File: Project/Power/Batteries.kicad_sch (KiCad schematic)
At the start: 52 parts, among them J10 Battery, J11 Battery, J12 Battery, J9 Battery, Q3 SQJ138ELP, Q4 SQJ138ELP, Q5 SQJ138ELP, Q6 SQJ138ELP, U10 INA199B3DCKR, U11 TL331, U12 INA199B3DCKR, U13 TL331, U2 NCV68061, U3 NCV68061, U4 INA199B3DCKR, U5 TL331, U6 INA199B3DCKR, U7 TL331, U8 NCV68061, U9 NCV68061

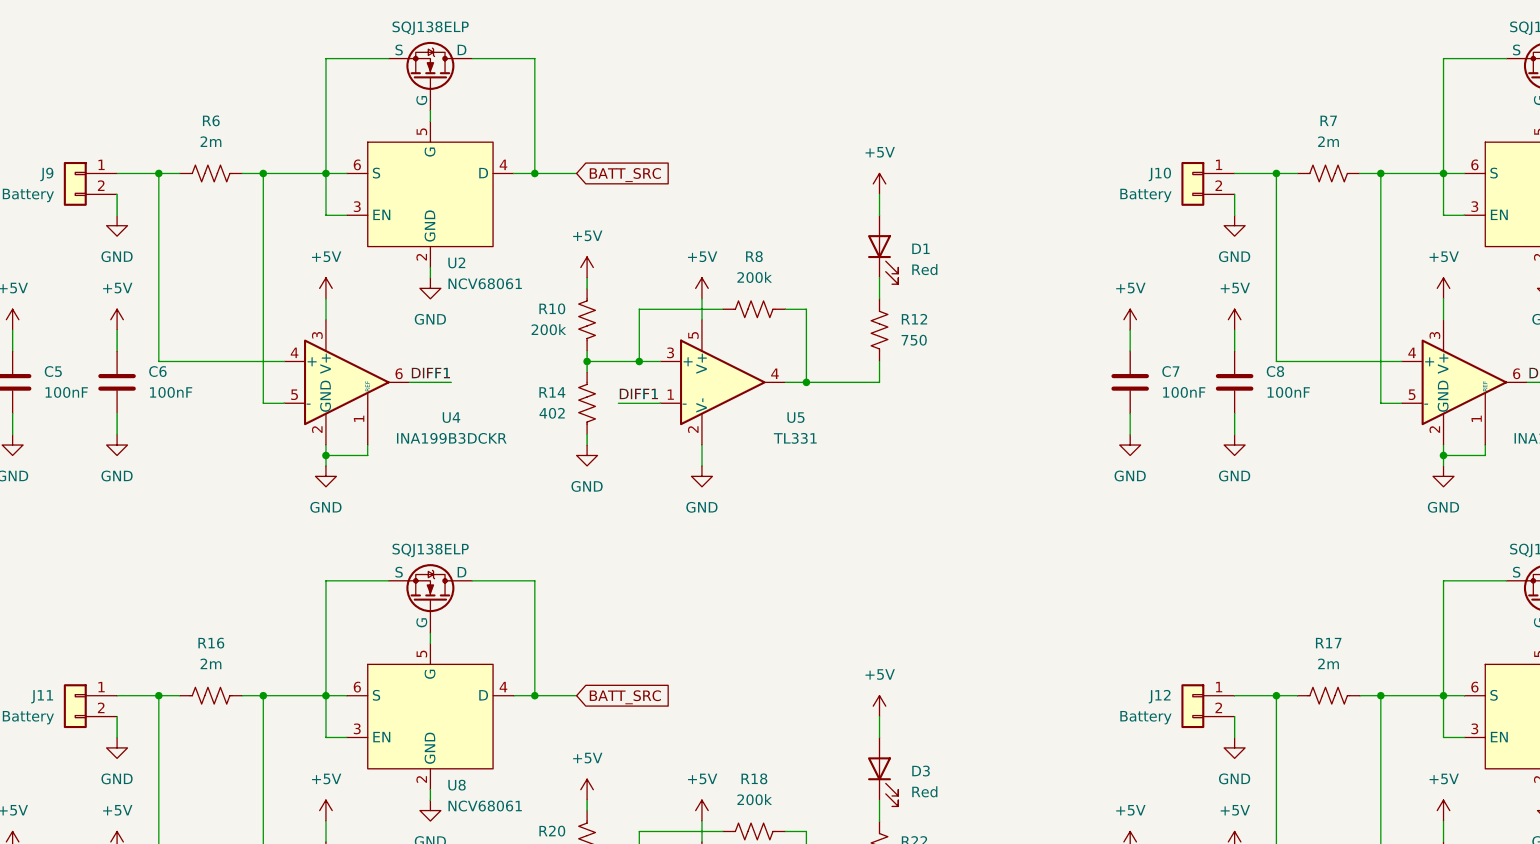
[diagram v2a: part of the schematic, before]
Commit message: Add INA226 sensors for batteries
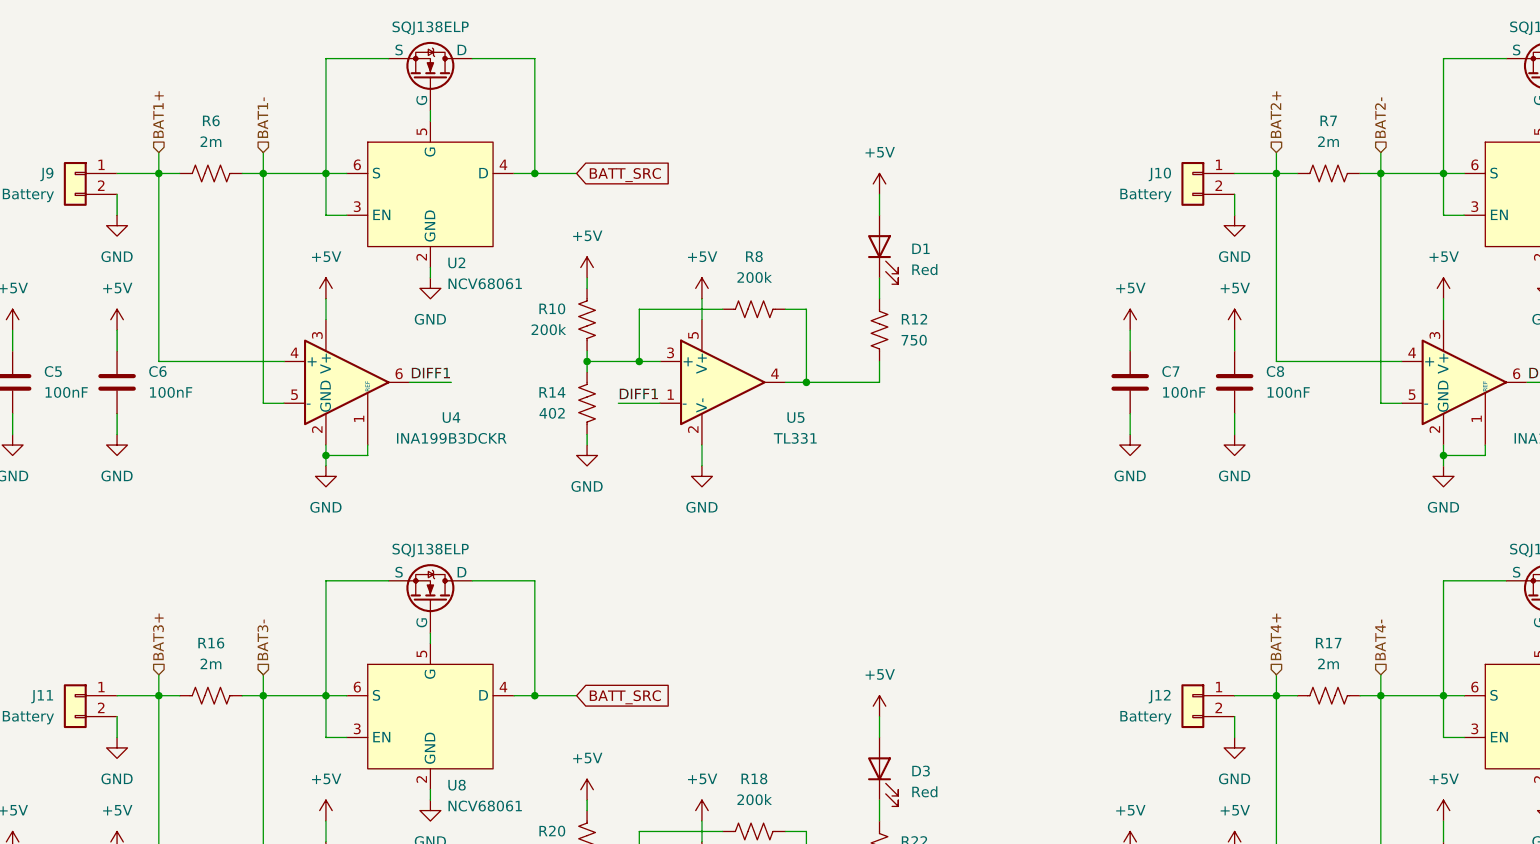
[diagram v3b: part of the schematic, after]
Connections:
- net BAT4-: now reaches Q6.1 (S), Q6.2 (S), Q6.3 (S), R17.2, U12.5 (-), U9.3 (EN), U9.6 (S)
- net BAT4+: now reaches J12.1 (Pin_1), R17.1, U12.4 (+)
- net BAT2+: now reaches J10.1 (Pin_1), R7.1, U6.4 (+)
- net BAT2-: now reaches Q4.1 (S), Q4.2 (S), Q4.3 (S), R7.2, U3.3 (EN), U3.6 (S), U6.5 (-)
- net BAT3-: now reaches Q5.1 (S), Q5.2 (S), Q5.3 (S), R16.2, U10.5 (-), U8.3 (EN), U8.6 (S)
- net BAT3+: now reaches J11.1 (Pin_1), R16.1, U10.4 (+)
- net BAT1-: now reaches Q3.1 (S), Q3.2 (S), Q3.3 (S), R6.2, U2.3 (EN), U2.6 (S), U4.5 (-)
- net BAT1+: now reaches J9.1 (Pin_1), R6.1, U4.4 (+)
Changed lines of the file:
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@@
+	(wire
+		(pts
+			(xy 191.77 99.06) (xy 191.77 101.6)
+		)
+		(stroke
+			(width 0)
+			(type default)
+		)
+	)
 	(wire
 		(pts
@@
 	(wire
 		(pts
+			(xy 55.88 99.06) (xy 55.88 101.6)
+		)
+		(stroke
+			(width 0)
+			(type default)
+		)
+	)
+	(wire
+		(pts
 			(xy 58.42 124.46) (xy 43.18 124.46)
 		)
@@
 	(wire
 		(pts
+			(xy 55.88 35.56) (xy 55.88 38.1)
+		)
+		(stroke
+			(width 0)
+			(type default)
+		)
+	)
+	(wire
+		(pts
 			(xy 204.47 71.12) (xy 204.47 72.39)
 		)
@@
 	(wire
 		(pts
+			(xy 43.18 35.56) (xy 43.18 38.1)
+		)
+		(stroke
+			(width 0)
+			(type default)
+		)
+	)
+	(wire
+		(pts
 			(xy 199.39 43.18) (xy 199.39 38.1)
 		)
@@
 	(wire
 		(pts
+			(xy 191.77 35.56) (xy 191.77 38.1)
+		)
+		(stroke
+			(width 0)
+			(type default)
+		)
+	)
+	(wire
+		(pts
 			(xy 68.58 134.62) (xy 68.58 135.89)
 		)
@@
 	(wire
 		(pts
+			(xy 179.07 35.56) (xy 179.07 38.1)
+		)
+		(stroke
+			(width 0)
+			(type default)
+		)
+	)
+	(wire
+		(pts
 			(xy 63.5 43.18) (xy 63.5 38.1)
 		)
@@
 	(wire
 		(pts
+			(xy 179.07 99.06) (xy 179.07 101.6)
+		)
+		(stroke
+			(width 0)
+			(type default)
+		)
+	)
+	(wire
+		(pts
 			(xy 119.38 63.5) (xy 121.92 63.5)
 		)
@@
 		(pts
 			(xy 199.39 134.62) (xy 199.39 135.89)
+		)
+		(stroke
+			(width 0)
+			(type default)
+		)
+	)
+	(wire
+		(pts
+			(xy 43.18 99.06) (xy 43.18 101.6)
 		)
 		(stroke
@@
 		)
 	)
+	(hierarchical_label "BAT1-"
+		(shape input)
+		(at 55.88 35.56 90)
+		(effects
+			(font
+				(size 1.27 1.27)
+			)
+			(justify left)
+		)
+	)
+	(hierarchical_label "BAT4+"
+		(shape input)
+		(at 179.07 99.06 90)
+		(effects
+			(font
+				(size 1.27 1.27)
+			)
+			(justify left)
+		)
+	)
+	(hierarchical_label "BAT2-"
+		(shape input)
+		(at 191.77 35.56 90)
+		(effects
+			(font
+				(size 1.27 1.27)
+			)
+			(justify left)
+		)
+	)
+	(hierarchical_label "BAT1+"
+		(shape input)
+		(at 43.18 35.56 90)
+		(effects
+			(font
+				(size 1.27 1.27)
+			)
+			(justify left)
+		)
+	)
+	(hierarchical_label "BAT3-"
+		(shape input)
+		(at 55.88 99.06 90)
+		(effects
+			(font
+				(size 1.27 1.27)
+			)
+			(justify left)
+		)
+	)
+	(hierarchical_label "BAT4-"
+		(shape input)
+		(at 191.77 99.06 90)
+		(effects
+			(font
+				(size 1.27 1.27)
+			)
+			(justify left)
+		)
+	)
+	(hierarchical_label "BAT2+"
+		(shape input)
+		(at 179.07 35.56 90)
+		(effects
+			(font
+				(size 1.27 1.27)
+			)
+			(justify left)
+		)
+	)
+	(hierarchical_label "BAT3+"
+		(shape input)
+		(at 43.18 99.06 90)
+		(effects
+			(font
+				(size 1.27 1.27)
+			)
+			(justify left)
+		)
+	)

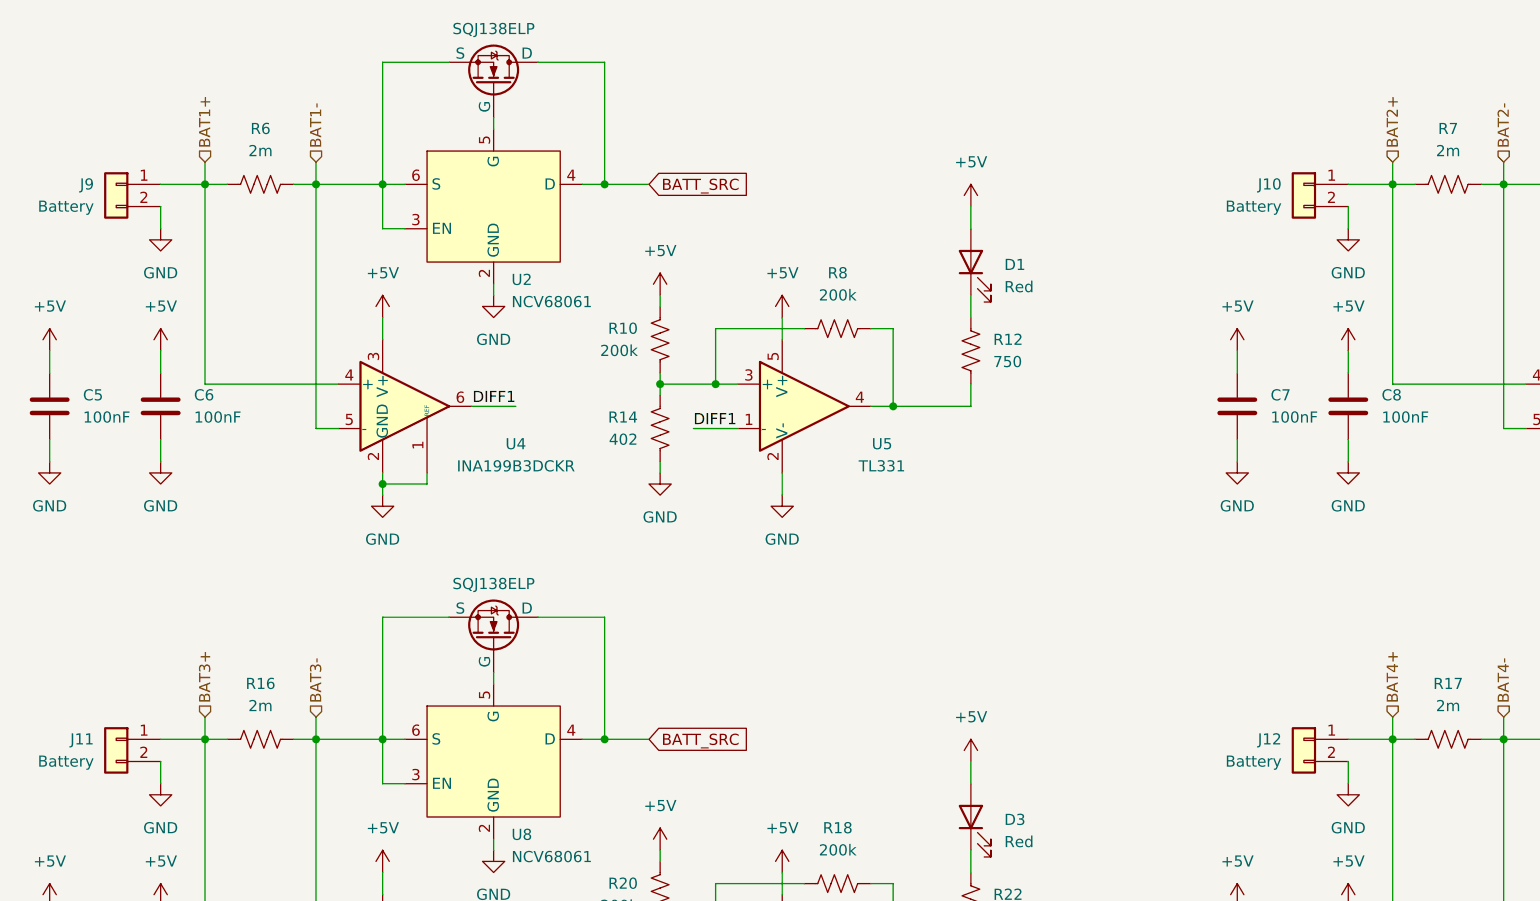
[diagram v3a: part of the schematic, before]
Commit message: Add power flags to battery inputs
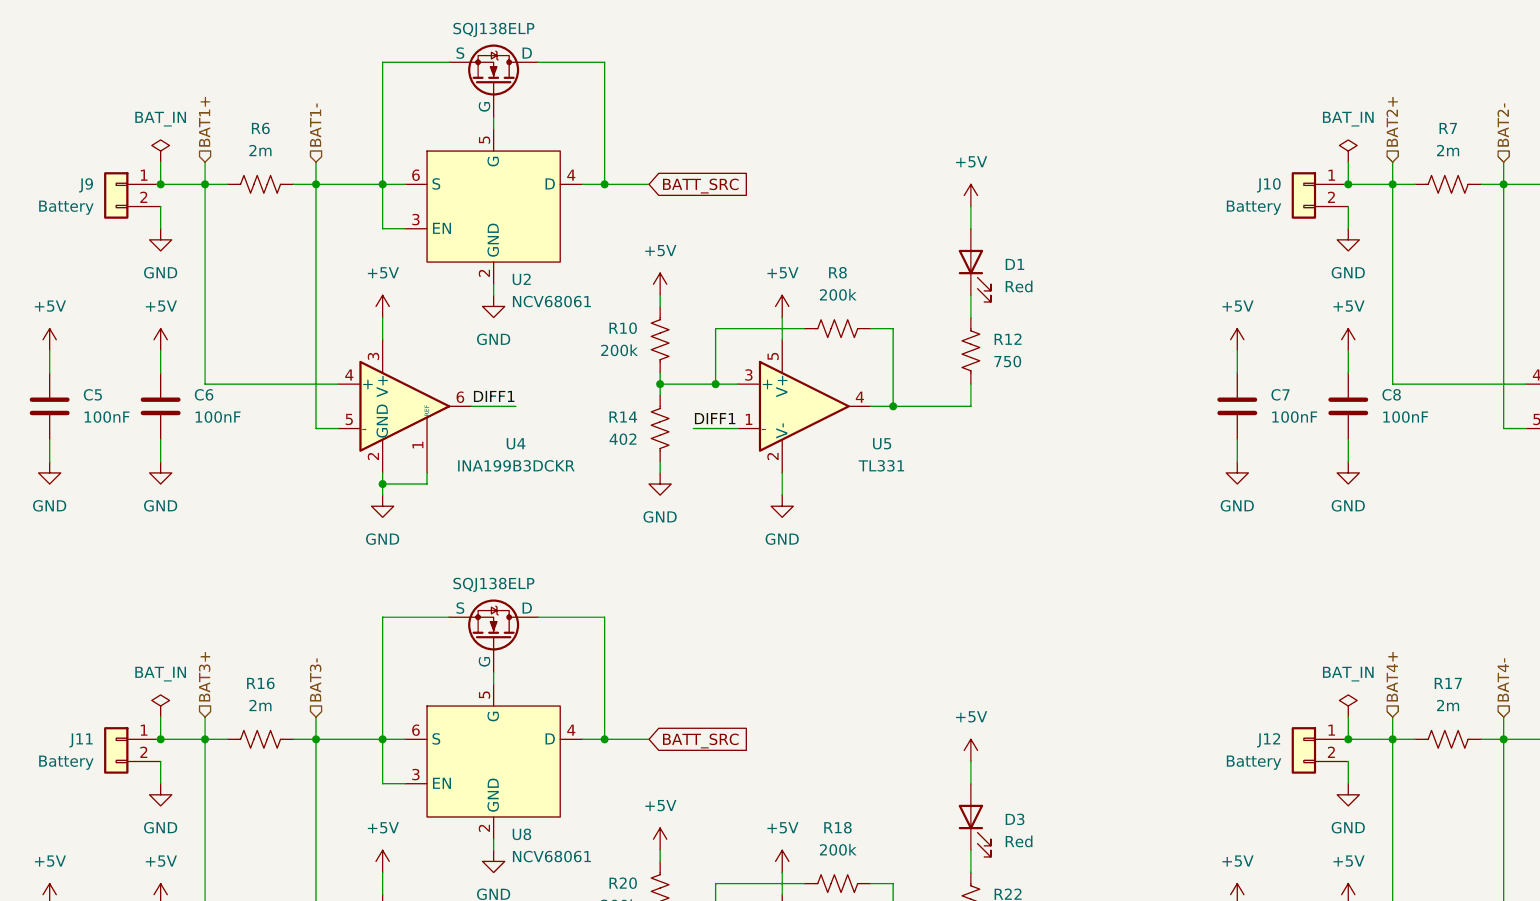
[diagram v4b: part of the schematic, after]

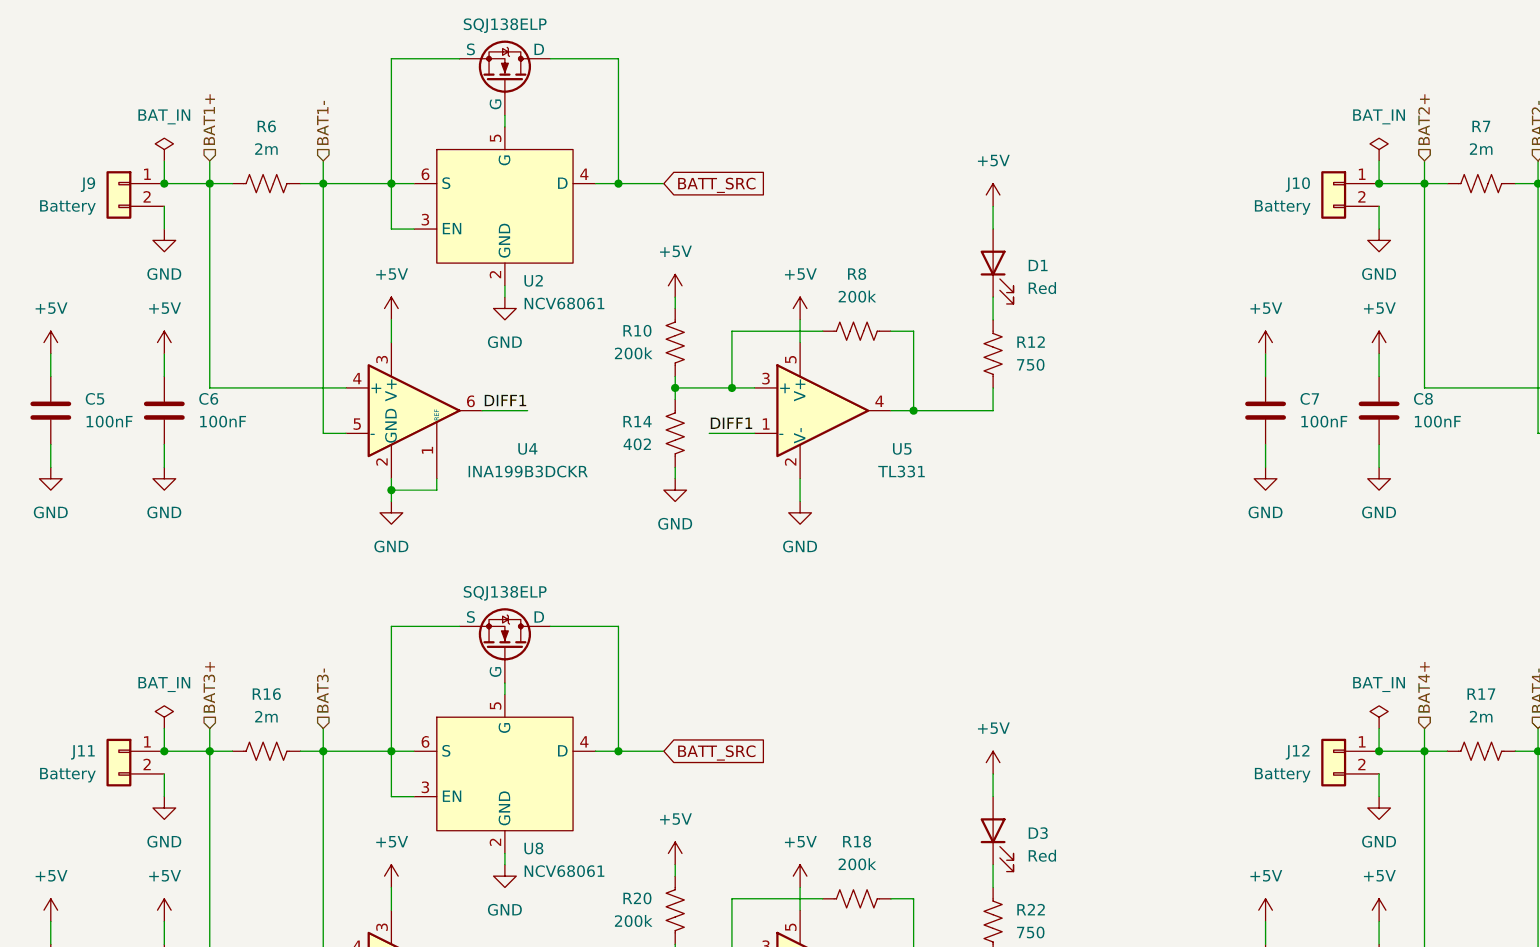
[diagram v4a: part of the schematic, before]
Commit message: Flip XT60 pin connections
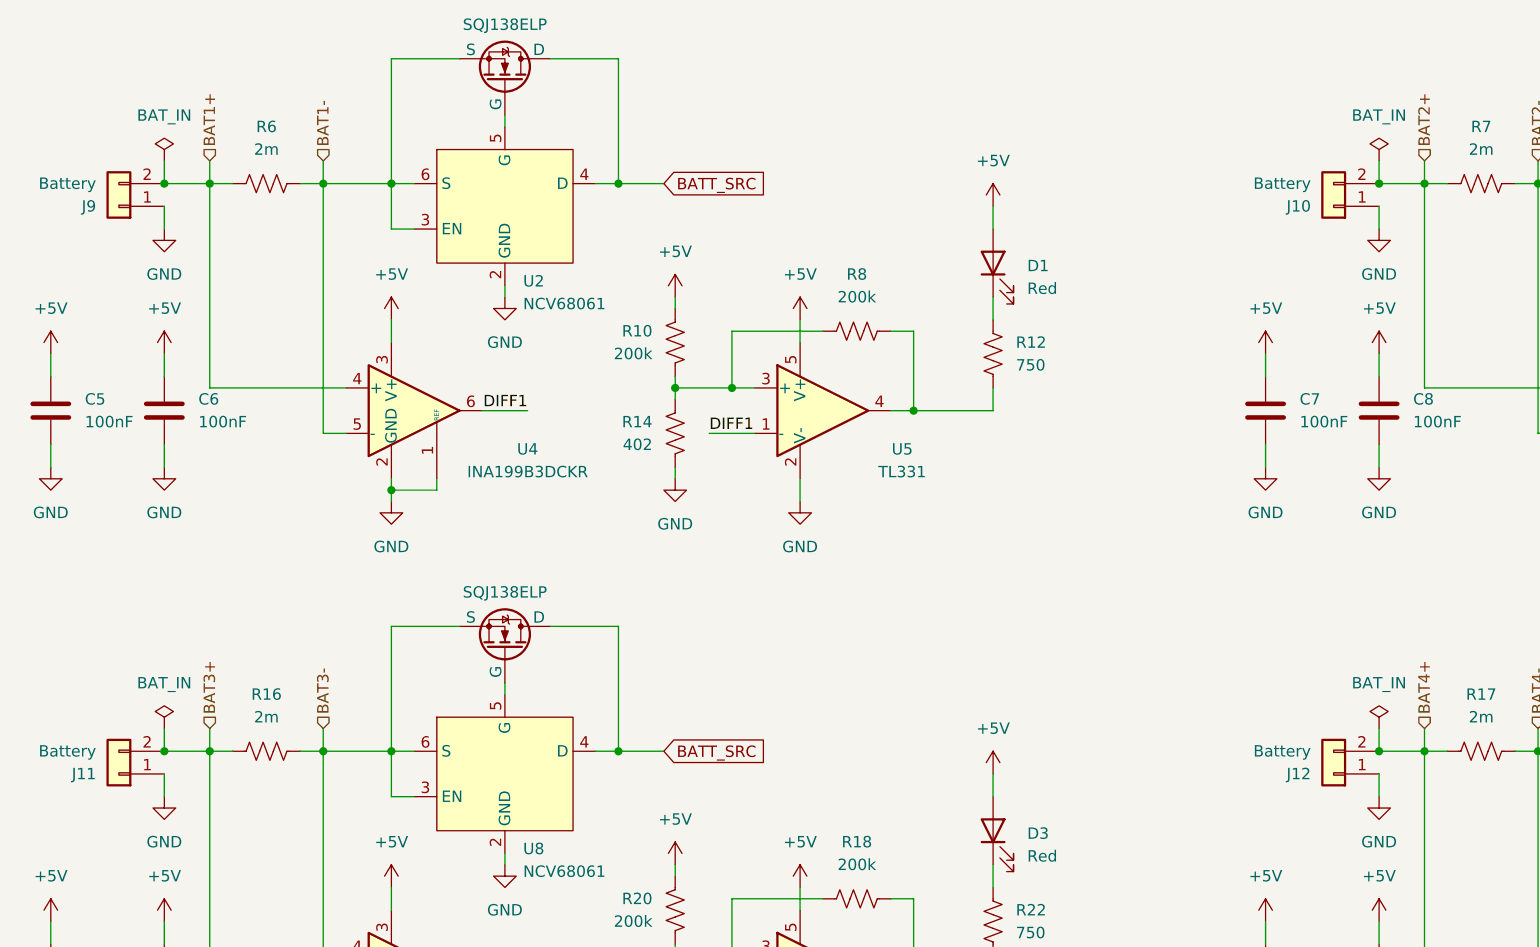
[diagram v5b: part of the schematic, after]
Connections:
- net BAT1+: now also J9.2 (Pin_2); no longer J9.1 (Pin_1)
- net BAT2+: now also J10.2 (Pin_2); no longer J10.1 (Pin_1)
- net BAT3+: now also J11.2 (Pin_2); no longer J11.1 (Pin_1)
- net BAT4+: now also J12.2 (Pin_2); no longer J12.1 (Pin_1)
- net GND: now also J10.1 (Pin_1), J11.1 (Pin_1), J12.1 (Pin_1), J9.1 (Pin_1); no longer J10.2 (Pin_2), J11.2 (Pin_2), J12.2 (Pin_2), J9.2 (Pin_2)
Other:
- moved on the sheet: J10, J11, J12, J9
